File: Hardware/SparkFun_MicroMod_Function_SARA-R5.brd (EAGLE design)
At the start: 37.5 x 65 mm, 115 parts, among them IC2 SN74AVC4T774PW, J1 MICROMOD_FUNCTION_STANDARD, J2 U.FL, J4 U.FL, J9 NANO_SIM, Q2 310mA/60V/1.6Ω, Q3 310mA/60V/1.6Ω, Q5 310mA/60V/1.6Ω, Q6 310mA/60V/1.6Ω, U1 SARA-R510M8S, U11 74HC1G04, U3 3.3V, U4 EEPROM, U8 AP7361C-33FGE

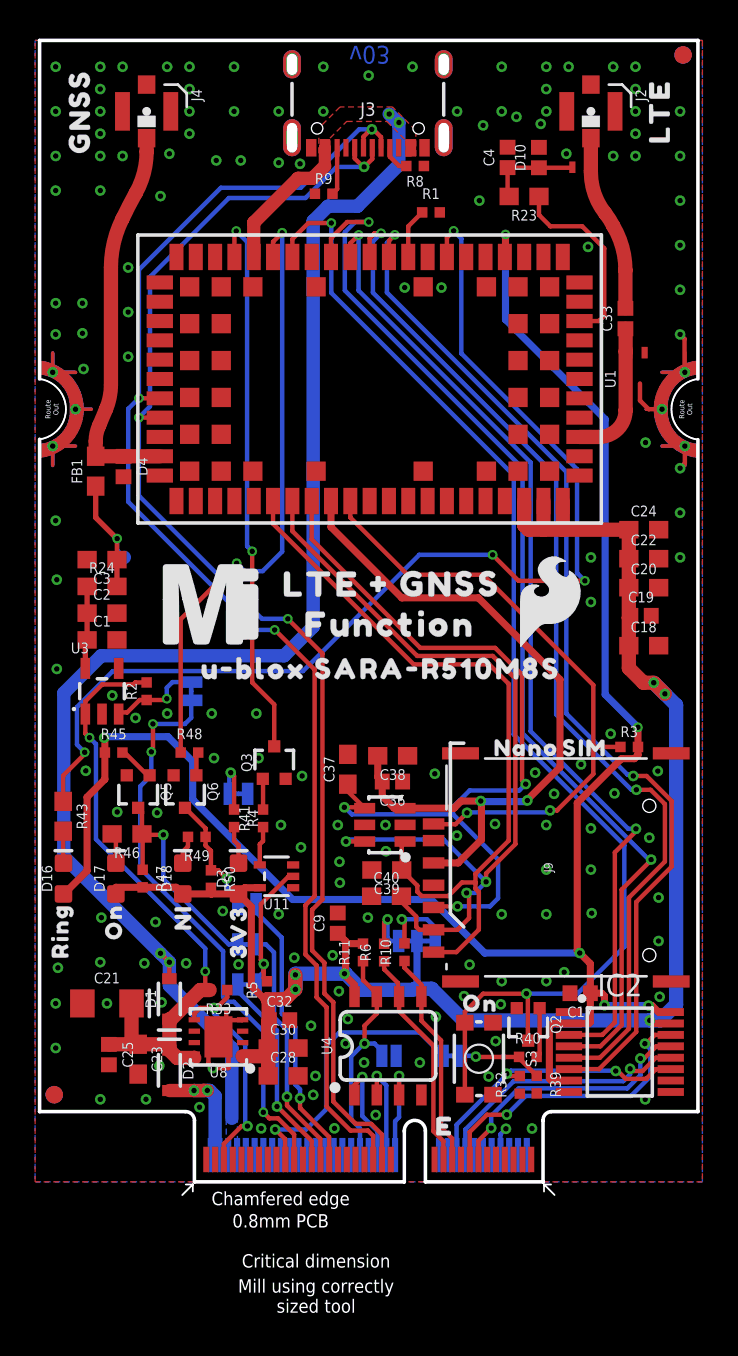
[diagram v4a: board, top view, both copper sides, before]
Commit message: USB D+ and D- routing
-re-did calcs and changed to 9 mil width with 8 mil spacing.
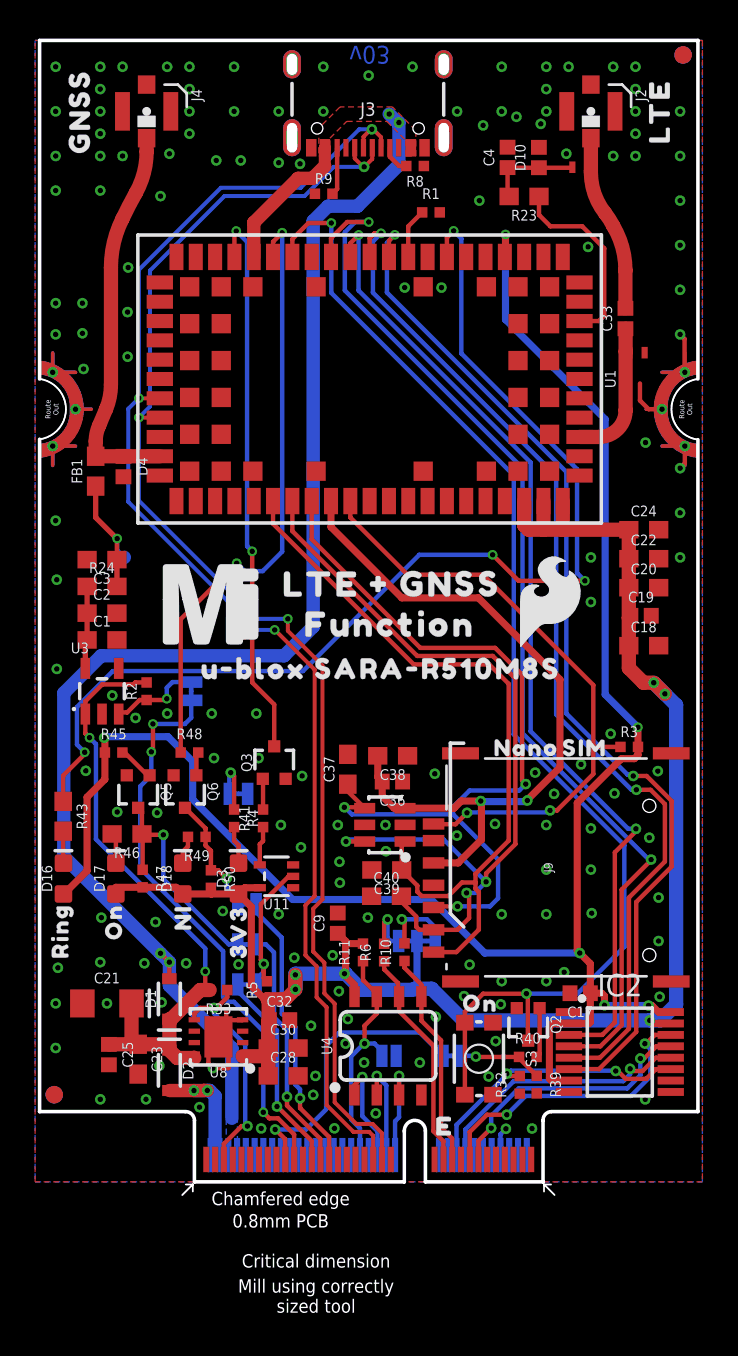
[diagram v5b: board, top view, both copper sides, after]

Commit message: update LEDs and limiting resistor values to new standards
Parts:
- R4: value 1k -> 4.7k
- R43: value 220 -> 240
- R46: value 100 -> 330
- R49: value 1k -> 2.2k
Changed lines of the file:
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@@
 <setting verticaltext="up"/>
 </settings>
-<grid distance="0.05" unitdist="inch" unit="inch" style="lines" multiple="1" display="yes" altdistance="0.0001" altunitdist="inch" altunit="inch"/>
+<grid distance="0.05" unitdist="inch" unit="inch" style="lines" multiple="1" display="yes" altdistance="0.005" altunitdist="inch" altunit="inch"/>
 <layers>
 <layer number="1" name="Top" color="4" fill="1" visible="yes" active="yes"/>
@@
 <layer number="19" name="Unrouted" color="6" fill="1" visible="yes" active="yes"/>
 <layer number="20" name="Dimension" color="24" fill="1" visible="yes" active="yes"/>
-<layer number="21" name="tPlace" color="16" fill="1" visible="no" active="yes"/>
-<layer number="22" name="bPlace" color="14" fill="1" visible="no" active="yes"/>
-<layer number="23" name="tOrigins" color="15" fill="1" visible="no" active="yes"/>
-<layer number="24" name="bOrigins" color="15" fill="1" visible="no" active="yes"/>
+<layer number="21" name="tPlace" color="16" fill="1" visible="yes" active="yes"/>
+<layer number="22" name="bPlace" color="14" fill="1" visible="yes" active="yes"/>
+<layer number="23" name="tOrigins" color="15" fill="1" visible="yes" active="yes"/>
+<layer number="24" name="bOrigins" color="15" fill="1" visible="yes" active="yes"/>
 <layer number="25" name="tNames" color="7" fill="1" visible="no" active="yes"/>
 <layer number="26" name="bNames" color="7" fill="1" visible="no" active="yes"/>
@@
 <attribute name="VALUE" x="33.2994" y="3.583" size="1.27" layer="27" align="center"/>
 </element>
-<element name="R49" library="SparkFun-Resistors" package="0402-TIGHT" value="1k" x="9.20655625" y="19.6469" smashed="yes" rot="R180">
+<element name="R49" library="SparkFun-Resistors" package="0402-TIGHT" value="2.2k" x="9.20655625" y="19.6469" smashed="yes" rot="R180">
 <attribute name="NAME" x="9.20655625" y="18.8849" size="0.6096" layer="25" font="vector" ratio="20" rot="R180" align="bottom-center"/>
-<attribute name="PROD_ID" value="RES-14342" x="73.97655625" y="161.8869" size="1.778" layer="27" font="vector" ratio="15" rot="R180" display="off"/>
-<attribute name="VALUE" x="9.20655625" y="20.4089" size="0.6096" layer="27" font="vector" ratio="20" rot="R180" align="top-center"/>
+<attribute name="PROD_ID" value="RES-14341" x="73.97655625" y="161.8869" size="1.778" layer="27" font="vector" ratio="15" rot="R180" display="off"/>
+<attribute name="VALUE" value="2.2k" x="9.20655625" y="20.4089" size="0.6096" layer="27" font="vector" ratio="20" rot="R180" align="top-center"/>
 </element>
 <element name="D16" library="SparkFun-LED" package="LED-0603" value="RED" x="1.6145" y="17.272" smashed="yes" rot="R90">
 <attribute name="NAME" x="0.9795" y="17.272" size="0.6096" layer="25" font="vector" ratio="20" rot="R90" align="bottom-center"/>
-<attribute name="PROD_ID" value="DIO-00819" x="147.6645" y="-79.248" size="1.778" layer="27" font="vector" ratio="15" rot="R90" display="off"/>
-<attribute name="VALUE" x="2.2495" y="17.272" size="0.6096" layer="27" font="vector" ratio="20" rot="R90" align="top-center"/>
-</element>
-<element name="R43" library="SparkFun-Resistors" library_urn="urn:adsk.eagle:library:532" package="0603" package3d_urn="urn:adsk.eagle:package:39650/1" value="220" x="1.597659375" y="20.8169" smashed="yes" rot="R270">
+<attribute name="PROD_ID" value="DIO-17976" x="147.6645" y="-79.248" size="1.778" layer="27" font="vector" ratio="15" rot="R90" display="off"/>
+</element>
+<element name="R43" library="SparkFun-Resistors" package="0603" value="240" x="1.597659375" y="20.8169" smashed="yes" rot="R270">
 <attribute name="NAME" x="2.359659375" y="20.8169" size="0.6096" layer="25" font="vector" ratio="20" rot="R270" align="bottom-center"/>
-<attribute name="PROD_ID" value="RES-07861" x="-152.072340625" y="123.6869" size="1.778" layer="27" font="vector" ratio="15" rot="R270" display="off"/>
-<attribute name="VALUE" value="220" x="0.835659375" y="20.8169" size="0.6096" layer="27" font="vector" ratio="20" rot="R270" align="top-center"/>
+<attribute name="PROD_ID" value="RES-07849" x="-152.072340625" y="123.6869" size="1.778" layer="27" font="vector" ratio="15" rot="R270" display="off"/>
+<attribute name="VALUE" value="240" x="0.835659375" y="20.8169" size="0.6096" layer="27" font="vector" ratio="20" rot="R270" align="top-center"/>
 </element>
 <element name="D17" library="SparkFun-LED" package="LED-0603" value="GREEN" x="4.599" y="17.272" smashed="yes" rot="R90">
@@
 <attribute name="VALUE" x="5.234" y="17.272" size="0.6096" layer="27" font="vector" ratio="20" rot="R90" align="top-center"/>
 </element>
-<element name="R46" library="SparkFun-Resistors" package="0603" value="100" x="5.234" y="19.812" smashed="yes" rot="R180">
+<element name="R46" library="SparkFun-Resistors" package="0603" value="330" x="5.234" y="19.812" smashed="yes" rot="R180">
 <attribute name="NAME" x="5.234" y="19.05" size="0.6096" layer="25" font="vector" ratio="20" rot="R180" align="bottom-center"/>
-<attribute name="PROD_ID" value="RES-07863" x="119.534" y="181.102" size="1.778" layer="27" font="vector" ratio="15" rot="R180" display="off"/>
-<attribute name="VALUE" x="5.234" y="20.574" size="0.6096" layer="27" font="vector" ratio="20" rot="R180" align="top-center"/>
+<attribute name="PROD_ID" value="RES-00818" x="119.534" y="181.102" size="1.778" layer="27" font="vector" ratio="15" rot="R180" display="off"/>
+<attribute name="VALUE" value="330" x="5.234" y="20.574" size="0.6096" layer="27" font="vector" ratio="20" rot="R180" align="top-center"/>
 </element>
 <element name="C24" library="HPG_Solution" package="0603" package3d_urn="urn:adsk.eagle:package:37414/1" value="8.2pF" x="34.6599" y="37.137340625" smashed="yes">
@@
 <attribute name="VALUE" x="22.5425" y="54.4465" size="0.6096" layer="27" font="vector" ratio="20" align="top-center"/>
 </element>
-<element name="R4" library="SparkFun-Resistors" package="0402-TIGHT" value="1k" x="11.33" y="20.701" smashed="yes" rot="R270">
+<element name="R4" library="SparkFun-Resistors" package="0402-TIGHT" value="4.7k" x="11.33" y="20.701" smashed="yes" rot="R270">
 <attribute name="NAME" x="12.092" y="20.701" size="0.6096" layer="25" font="vector" ratio="20" rot="R270" align="bottom-center"/>
-<attribute name="PROD_ID" value="RES-14342" x="11.33" y="20.701" size="1.778" layer="27" font="vector" ratio="15" rot="R270" display="off"/>
-<attribute name="VALUE" x="10.568" y="20.701" size="0.6096" layer="27" font="vector" ratio="20" rot="R270" align="top-center"/>
+<attribute name="PROD_ID" value="RES-15343" x="11.33" y="20.701" size="1.778" layer="27" font="vector" ratio="15" rot="R270" display="off"/>
+<attribute name="VALUE" value="4.7k" x="10.568" y="20.701" size="0.6096" layer="27" font="vector" ratio="20" rot="R270" align="top-center"/>
 </element>
 <element name="D3" library="SparkFun-LED" package="LED-0603" value="RED" x="11.584" y="17.272" smashed="yes" rot="R90">
 <attribute name="NAME" x="10.949" y="17.272" size="0.6096" layer="25" font="vector" ratio="20" rot="R90" align="bottom-center"/>
-<attribute name="PROD_ID" value="DIO-00819" x="11.584" y="17.272" size="1.778" layer="27" font="vector" ratio="15" rot="R90" display="off"/>
-<attribute name="VALUE" x="12.219" y="17.272" size="0.6096" layer="27" font="vector" ratio="20" rot="R90" align="top-center"/>
+<attribute name="PROD_ID" value="DIO-17976" x="11.584" y="17.272" size="1.778" layer="27" font="vector" ratio="15" rot="R90" display="off"/>
 </element>
 <element name="U$29" library="HPG_Solution" package="NI0" value="" x="8.4185" y="15.0495" smashed="yes" rot="R90"/>

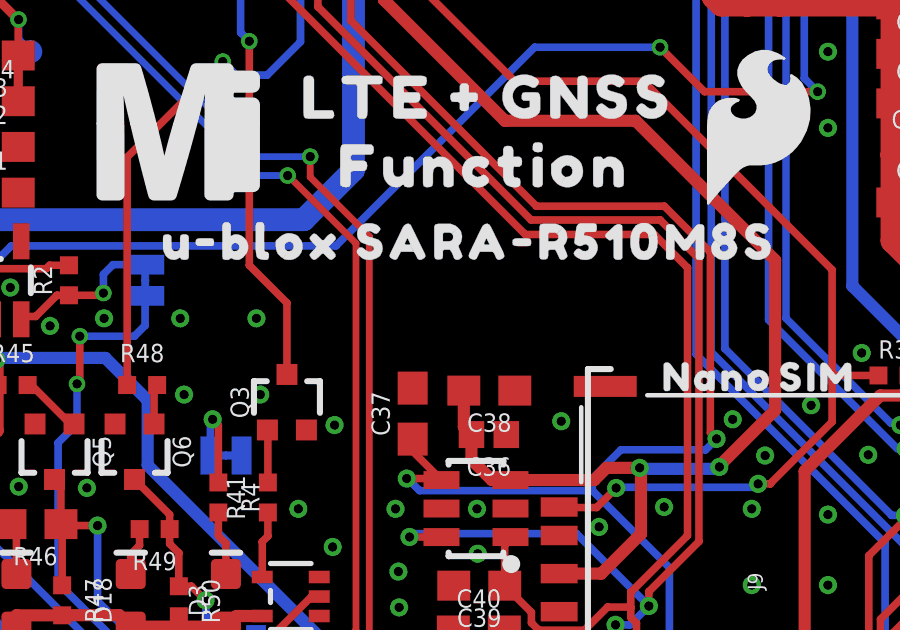
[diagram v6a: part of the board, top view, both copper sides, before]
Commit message: added oshw logo
-also added label to ANT_REG_EN jumper
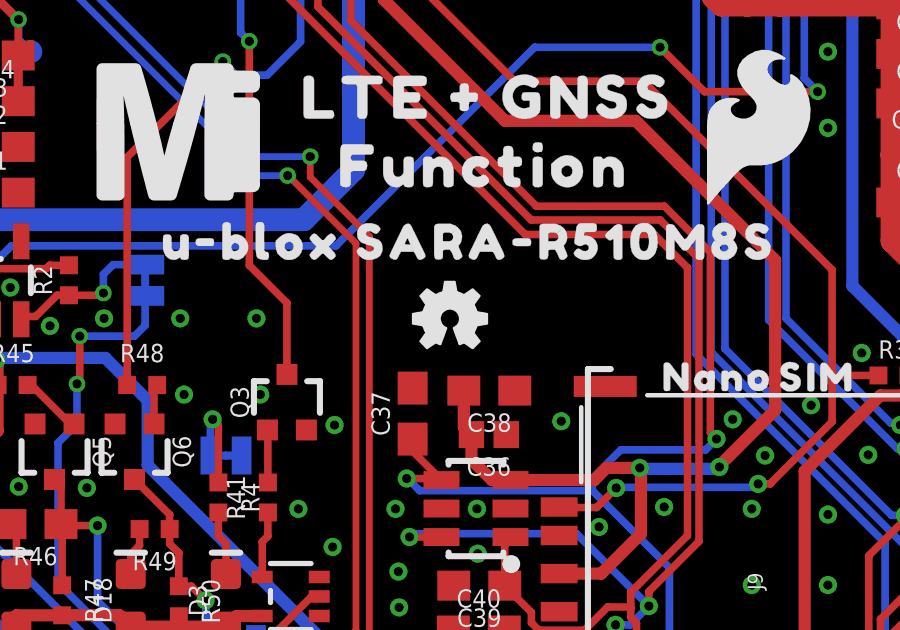
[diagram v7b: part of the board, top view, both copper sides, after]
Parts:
- removed U$4: (no value), output:LTE_FUNCTION0
- added LOGO4, LOGO6: OSHW-LOGOMINI, SparkFun-Aesthetics:OSHW-LOGO-MINI
- added U$19: (no value), output:FUNCTION0
- added U$2: (no value), output:#ANT_REG_EN#0
- added U$20: (no value), output:U#BLOX_SARA#R510M8S0
- U$14: device output:DESIGNED_BY_#MAZGCH_IN_SWITZERLAND3 -> output:LTE_#_GNSS0
- moved U$14 4.57 mm to (17.9, 38.2)
- moved U$3 0.46 mm to (17.8, 42.1)
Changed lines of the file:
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@@
 <drawing>
 <settings>
-<setting alwaysvectorfont="no"/>
+<setting alwaysvectorfont="yes"/>
 <setting verticaltext="up"/>
 </settings>
 <grid distance="0.05" unitdist="inch" unit="inch" style="lines" multiple="1" display="yes" altdistance="0.005" altunitdist="inch" altunit="inch"/>
 <layers>
-<layer number="1" name="Top" color="4" fill="1" visible="yes" active="yes"/>
+<layer number="1" name="Top" color="4" fill="1" visible="no" active="yes"/>
 <layer number="2" name="Route2" color="16" fill="1" visible="no" active="no"/>
 <layer number="3" name="Route3" color="17" fill="1" visible="no" active="no"/>
@@
 <layer number="17" name="Pads" color="2" fill="1" visible="yes" active="yes"/>
 <layer number="18" name="Vias" color="2" fill="1" visible="yes" active="yes"/>
-<layer number="19" name="Unrouted" color="6" fill="1" visible="yes" active="yes"/>
-<layer number="20" name="Dimension" color="24" fill="1" visible="yes" active="yes"/>
-<layer number="21" name="tPlace" color="16" fill="1" visible="yes" active="yes"/>
+<layer number="19" name="Unrouted" color="6" fill="1" visible="no" active="yes"/>
+<layer number="20" name="Dimension" color="24" fill="1" visible="no" active="yes"/>
+<layer number="21" name="tPlace" color="16" fill="1" visible="no" active="yes"/>
 <layer number="22" name="bPlace" color="14" fill="1" visible="yes" active="yes"/>
-<layer number="23" name="tOrigins" color="15" fill="1" visible="yes" active="yes"/>
+<layer number="23" name="tOrigins" color="15" fill="1" visible="no" active="yes"/>
 <layer number="24" name="bOrigins" color="15" fill="1" visible="yes" active="yes"/>
 <layer number="25" name="tNames" color="7" fill="1" visible="no" active="yes"/>
@@
 <layer number="43" name="vRestrict" color="2" fill="10" visible="no" active="yes"/>
 <layer number="44" name="Drills" color="7" fill="1" visible="no" active="yes"/>
-<layer number="45" name="Holes" color="7" fill="1" visible="yes" active="yes"/>
+<layer number="45" name="Holes" color="7" fill="1" visible="no" active="yes"/>
 <layer number="46" name="Milling" color="3" fill="1" visible="no" active="yes"/>
 <layer number="47" name="Measures" color="13" fill="1" visible="no" active="yes"/>
 <layer number="48" name="Document" color="7" fill="1" visible="no" active="yes"/>
-<layer number="49" name="Reference" color="23" fill="5" visible="yes" active="yes"/>
+<layer number="49" name="Reference" color="23" fill="5" visible="no" active="yes"/>
 <layer number="50" name="dxf" color="7" fill="1" visible="no" active="no"/>
-<layer number="51" name="tDocu" color="6" fill="1" visible="yes" active="yes"/>
+<layer number="51" name="tDocu" color="6" fill="1" visible="no" active="yes"/>
 <layer number="52" name="bDocu" color="7" fill="1" visible="no" active="yes"/>
 <layer number="53" name="tGND_GNDA" color="7" fill="9" visible="no" active="no"/>
@@
 <layer number="98" name="Guide" color="6" fill="1" visible="no" active="no"/>
 <layer number="99" name="SpiceOrder" color="7" fill="1" visible="no" active="no"/>
-<layer number="100" name="Muster" color="7" fill="1" visible="yes" active="yes"/>
+<layer number="100" name="Muster" color="7" fill="1" visible="no" active="yes"/>
 <layer number="101" name="Patch_Top" color="12" fill="4" visible="no" active="no"/>
 <layer number="102" name="Vscore" color="7" fill="1" visible="no" active="no"/>
@@
 <element name="U$57" library="HPG_Solution" package="3V34" value="" x="11.5935" y="14.224" smashed="yes" rot="R90"/>
 <element name="U$80" library="output" package="RING0" value="" x="1.4335" y="14.2875" smashed="yes" rot="R90"/>
-<element name="U$14" library="output" package="DESIGNED_BY_#MAZGCH_IN_SWITZERLAND3" value="" x="18.71311875" y="33.72611875" smashed="yes" rot="MR0"/>
 <element name="U$18" library="output" package="NANO0" value="" x="27.983184375" y="24.718340625" smashed="yes"/>
 <element name="U$126" library="output" package="SIM0" value="" x="31.295340625" y="24.708175" smashed="yes"/>
@@
 </element>
 <element name="LOGO1" library="SparkFun-Aesthetics" package="SFE_LOGO_NAME_FLAME_.2" value="SFE_LOGO_NAME_FLAME.2_INCH" x="18.63598125" y="46.9011" smashed="yes" rot="MR0"/>
-<element name="U$3" library="SparkFun-MicroMod" package="MICROMOD_MI_LOGO_1" value="" x="18.026378125" y="41.7465" smashed="yes" rot="MR0"/>
-<element name="U$4" library="output" package="LTE_FUNCTION0" value="" x="17.848584375" y="37.321821875" smashed="yes" rot="MR0"/>
+<element name="U$3" library="SparkFun-MicroMod" package="MICROMOD_MI_LOGO_1" value="" x="17.772378125" y="42.1275" smashed="yes" rot="MR0"/>
 <element name="LOGO2" library="SparkFun-Aesthetics" package="SFE_LOGO_FLAME_.2" value="SFE_LOGO_FLAME.2_INCH" x="29.337" y="33.02" smashed="yes"/>
 <element name="R5" library="SparkFun-Resistors" package="0402-TIGHT" value="100k" x="13.208" y="10.922" smashed="yes" rot="R90">
@@
 <element name="U$16" library="output" package="LTE0" value="" x="35.56" y="60.96" smashed="yes" rot="R90"/>
 <element name="U$17" library="output" package="GNSS0" value="" x="2.54" y="60.96" smashed="yes" rot="R90"/>
+<element name="LOGO4" library="SparkFun-Aesthetics" package="OSHW-LOGO-MINI" value="OSHW-LOGOMINI" x="19.05" y="26.67" smashed="yes"/>
+<element name="U$14" library="output" package="LTE_#_GNSS0" value="" x="17.907" y="38.227" smashed="yes" rot="MR0"/>
+<element name="U$19" library="output" package="FUNCTION0" value="" x="17.907" y="36.195" smashed="yes" rot="MR0"/>
+<element name="U$20" library="output" package="U#BLOX_SARA#R510M8S0" value="" x="17.907" y="34.036" smashed="yes" rot="MR0"/>
+<element name="LOGO6" library="SparkFun-Aesthetics" package="OSHW-LOGO-MINI" value="OSHW-LOGOMINI" x="18.542" y="31.496" smashed="yes" rot="MR0"/>
+<element name="U$2" library="output" package="#ANT_REG_EN#0" value="" x="15.494" y="27.94" smashed="yes" rot="MR0"/>
 </elements>
 <signals>
